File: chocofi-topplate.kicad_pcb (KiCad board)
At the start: 2 copper layers, 111.4 x 90 mm, 23 parts, among them SW10 SW_PUSH, SW11 SW_PUSH, SW12 SW_PUSH, SW14 SW_PUSH, SW15 SW_PUSH, SW16 SW_PUSH, SW17 SW_PUSH, SW18 SW_PUSH, SW19 SW_PUSH, SW2 SW_PUSH, SW20 SW_PUSH, SW21 SW_PUSH, SW3 SW_PUSH, SW4 SW_PUSH, SW5 SW_PUSH, SW6 SW_PUSH, SW8 SW_PUSH, SW9 SW_PUSH

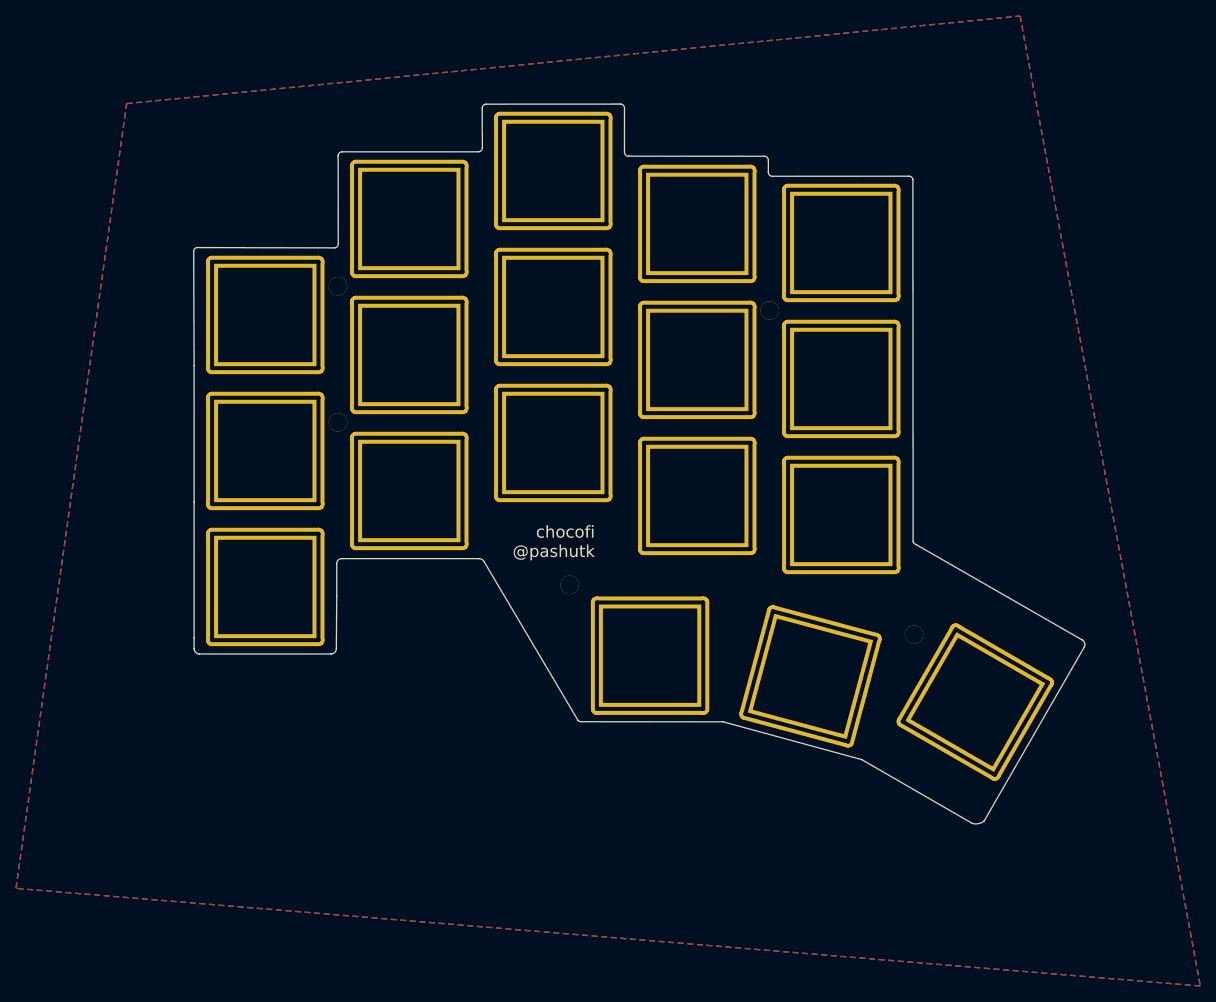
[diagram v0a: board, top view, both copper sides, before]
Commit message: Remove excessive corner pad surface, rm doorka logo
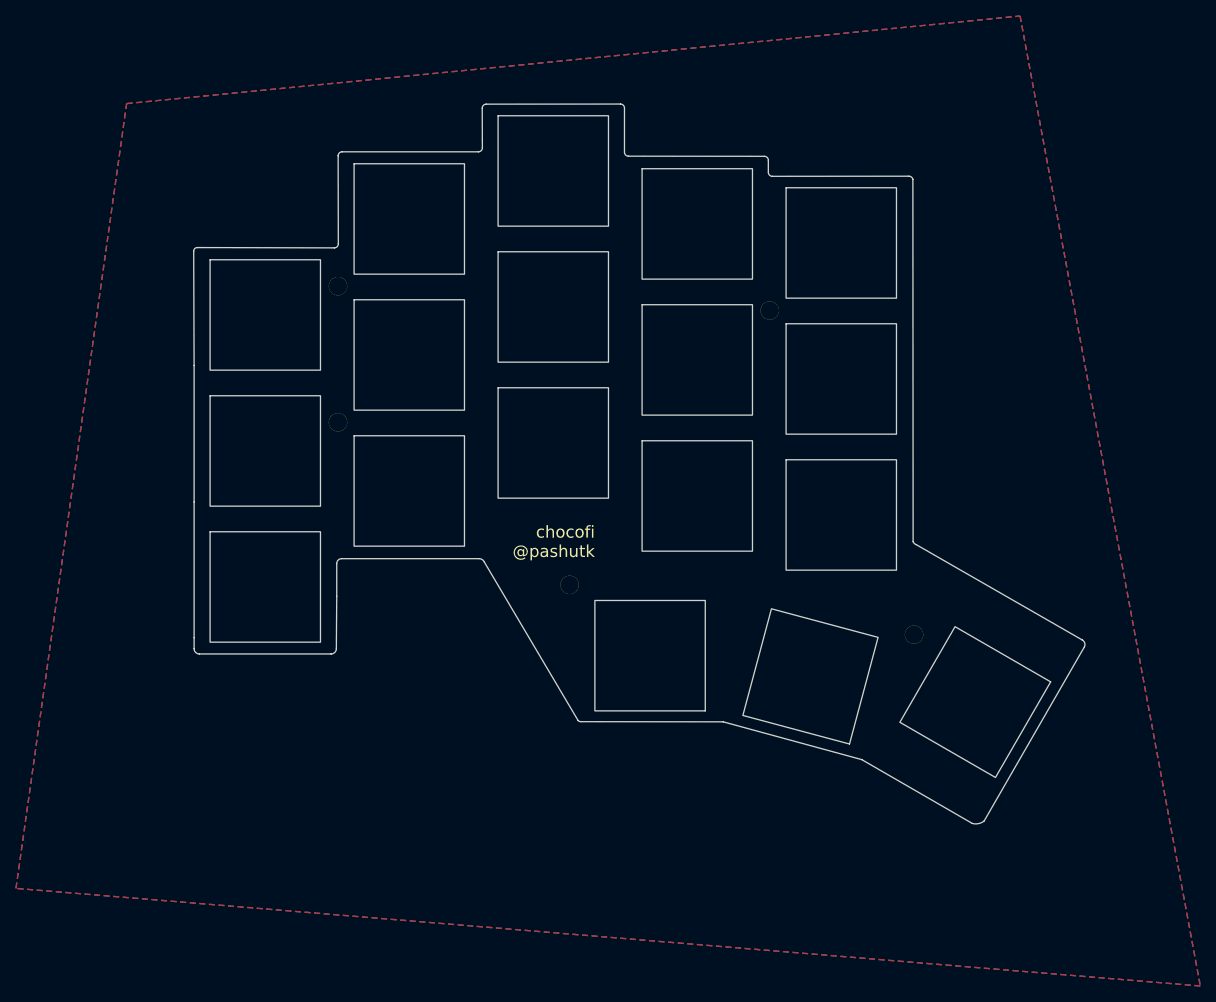
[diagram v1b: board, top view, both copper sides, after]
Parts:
- SW10, SW11, SW12, SW14, SW15, SW16, SW17, SW18, SW19, SW2, SW20, SW21, SW3, SW4, SW5, SW6, SW8, SW9: footprint kbd:SW_Hole_TH_choc -> kbd:SW_Hole_choc
